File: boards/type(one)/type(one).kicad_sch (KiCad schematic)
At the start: 37 parts, among them J1 IDC-Header, J2 IDC-Header, J3 Conn_01x02, J4 Conn_01x05, J5 Conn_01x05, J6 Conn_01x03, J7 Conn_01x02, Q1 2N2907, Q2 2n2222, Q3 IRF4905, Q4 2N3904, U1 ESP32-WROOM-UE, U2 LM393, U4 LM1117T-5.0, U5 LM1117T-3.3

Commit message: creating board
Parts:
- C10: footprint (none) -> Capacitor_THT:C_Disc_D6.0mm_W2.5mm_P5.00mm
- C3: footprint Capacitor_THT:C_Rect_L16.5mm_W4.9mm_P15.00mm_MKT -> Capacitor_THT:CP_Radial_Tantal_D5.5mm_P2.50mm
- C4, C5, C6: footprint (none) -> Capacitor_THT:CP_Radial_Tantal_D5.5mm_P2.50mm
- C9: footprint (none) -> Capacitor_THT:CP_Radial_Tantal_D6.0mm_P2.50mm
- D1: footprint (none) -> Diode_THT:D_DO-35_SOD27_P7.62mm_Horizontal
- D2: value 2n5060 -> TIC106; footprint (none) -> Package_TO_SOT_THT:TO-220-3_Vertical; symbol Device:Q_SCR_AGK -> Device:Q_SCR_KAG
- F1, J3, J7: footprint (none) -> Connector_Molex:Molex_KK-254_AE-6410-02A_1x02_P2.54mm_Vertical
- J1: value IDC-Header -> IDC-Header_02x03
- J2: value IDC-Header -> IDC-Header_02x05
- J4, J5: footprint (none) -> Connector_Molex:Molex_KK-254_AE-6410-05A_1x05_P2.54mm_Vertical
- J6: footprint (none) -> Connector_Molex:Molex_KK-254_AE-6410-03A_1x03_P2.54mm_Vertical
- Q4: value 2N3904 -> 2n2222
- U4: footprint Package_SON:WSON-8-1EP_4x4mm_P0.8mm_EP1.98x3mm_ThermalVias -> Package_TO_SOT_THT:TO-220-3_Vertical
- U5: footprint Package_TO_SOT_THT:TO-220-3_Horizontal_TabDown -> Package_TO_SOT_THT:TO-220-3_Vertical
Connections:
- net +5V: no longer J2.1 (Pin_1)
- net GND: now also D2.1 (K); no longer D2.3 (K)
- net at C8.1, F1.2, Q3.1 (D): now also D2.2 (A); no longer D2.1 (A)
- net at C7.1, D1.2 (A), Q3.2 (G)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: now also D2.3 (G); no longer D2.2 (G)
- new net +3.3V: J2.1 (Pin_1)
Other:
- note added: "Input voltage VDC 9V-12V"

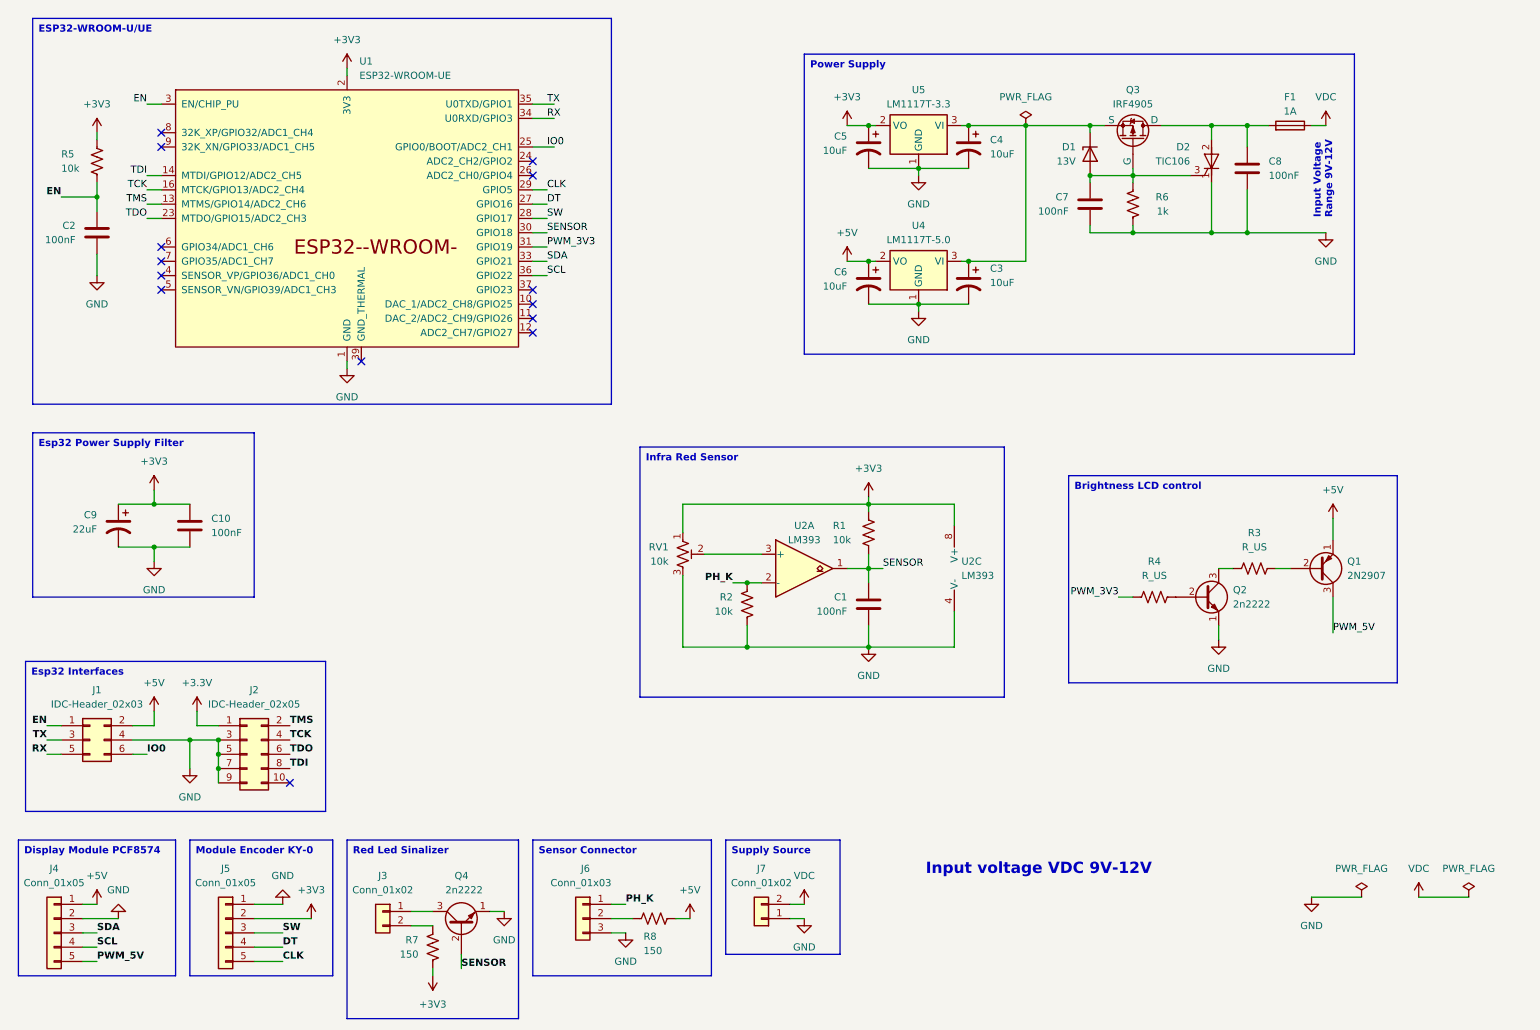
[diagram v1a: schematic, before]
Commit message: ajust sensor circuit
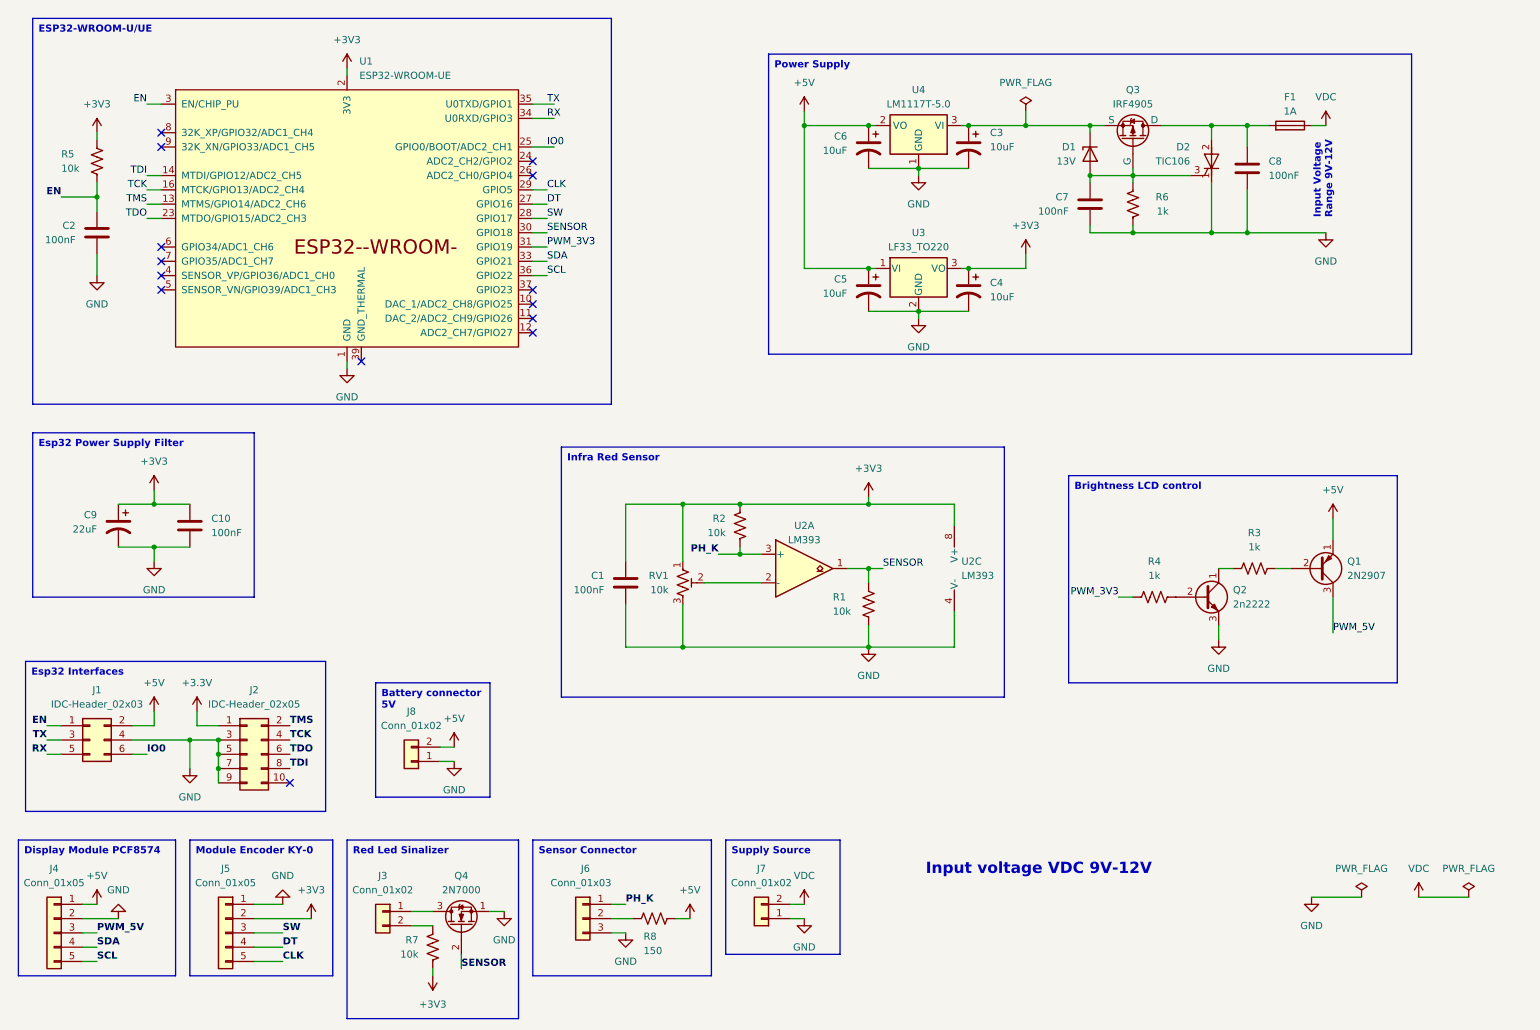
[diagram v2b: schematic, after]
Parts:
- removed Q4: 2n2222, Package_TO_SOT_THT:TO-92_Inline, symbol Transistor_BJT:2N3904
- removed U5: LM1117T-3.3, Package_TO_SOT_THT:TO-220-3_Vertical, symbol Regulator_Linear:LM1117T-3.3
- added J8: Conn_01x02, Connector_Molex:Molex_KK-254_AE-6410-02A_1x02_P2.54mm_Vertical, symbol Connector_Generic:Conn_01x02
- added Q4: 2N7000, Package_TO_SOT_THT:TO-92_Inline, symbol Transistor_FET:2N7000
- added U3: LF33_TO220, Package_TO_SOT_THT:TO-220-3_Vertical, symbol Regulator_Linear:LF33_TO220
- Q2: symbol Transistor_BJT:2N3904 -> Transistor_BJT:BC237
- R3, R4: value R_US -> 1k
- R7: value 150 -> 10k
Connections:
- net +3V3: now also C1.1, C4.1, R2.1, U3.3 (VO); no longer C5.1, R1.1
- net +5V: now also C5.1, J8.2 (Pin_2), U3.1 (VI)
- net GND: now also Q2.3 (E), R1.2, J8.1 (Pin_1), Q4.1 (S), U3.2 (GND); no longer Q2.1 (E), R2.2
- net PH_K: now also R2.2, U2.3 (+); no longer R2.1, U2.2 (-)
- net PWM_5V: now also J4.3 (Pin_3); no longer J4.5 (Pin_5)
- net SCL: now also J4.5 (Pin_5); no longer J4.4 (Pin_4)
- net SDA: now also J4.4 (Pin_4); no longer J4.3 (Pin_3)
- net SENSOR: now also R1.1, Q4.2 (G); no longer C1.1, R1.2
- net at RV1.2: now also U2.2 (-); no longer U2.3 (+)
- net at C3.1, D1.1 (K), Q3.3 (S)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: no longer C4.1
- net at R3.1: now also Q2.1 (C); no longer Q2.3 (C)
- net at J3.1 (Pin_1): now also Q4.3 (D)
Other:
- moved on the sheet: C1, C3, C4, C5, C6, R1, R2, RV1, U4

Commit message: add hysteresis on sensor
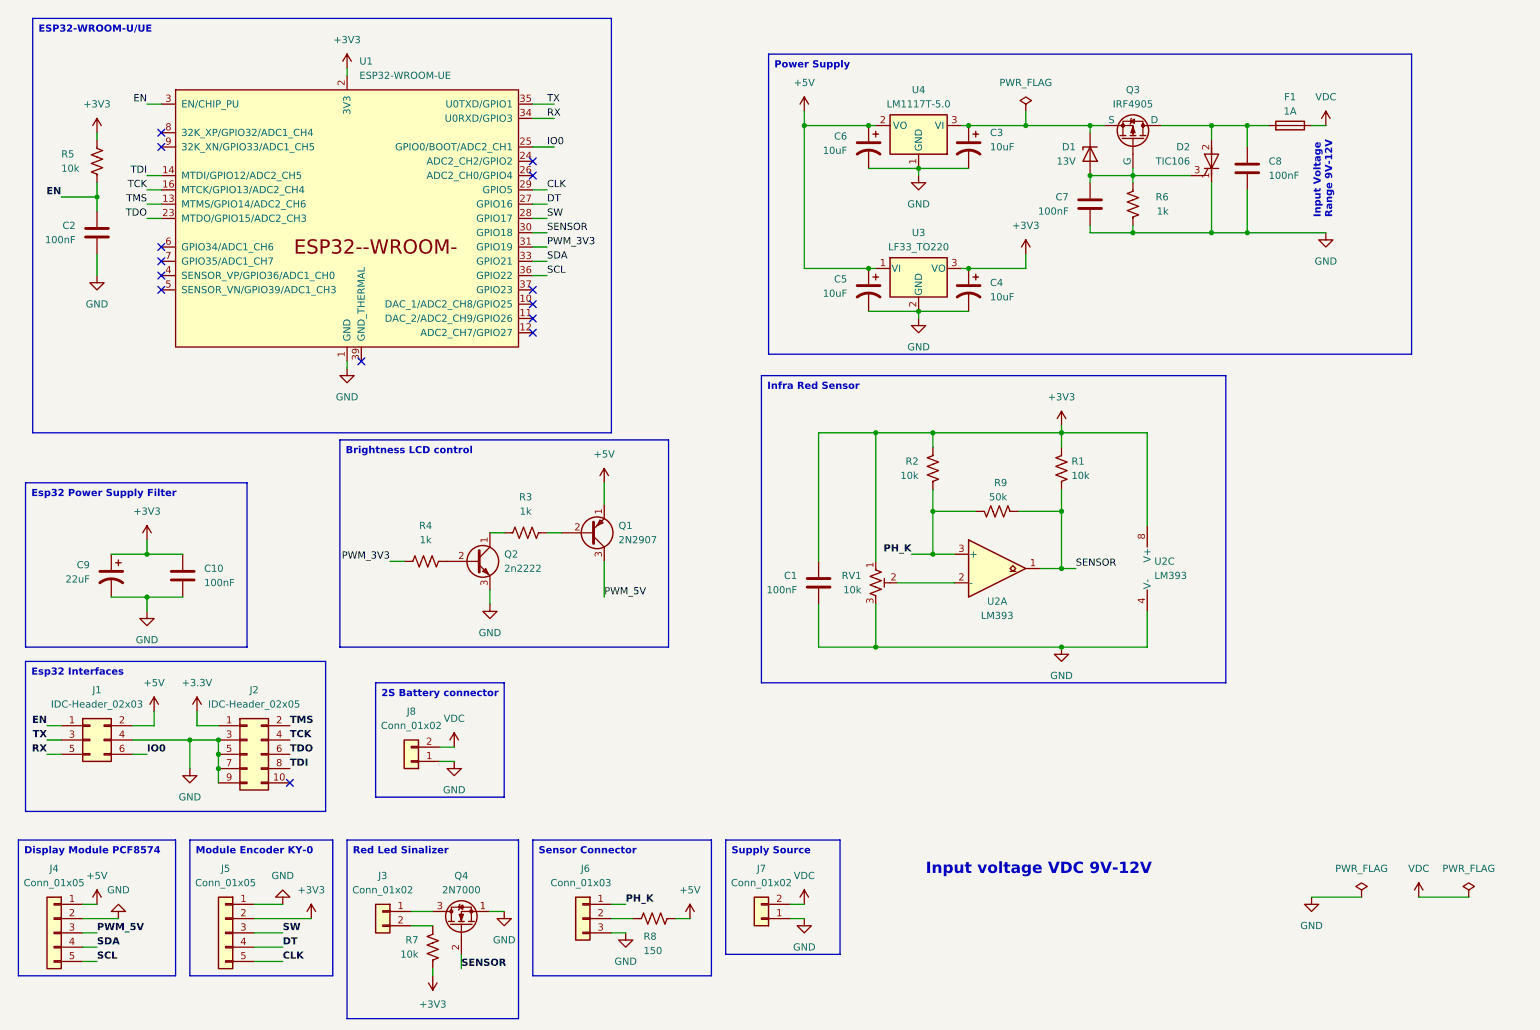
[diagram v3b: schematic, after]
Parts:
- added R9: 50k, Resistor_THT:R_Axial_DIN0207_L6.3mm_D2.5mm_P7.62mm_Horizontal, symbol Device:R_US
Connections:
- net +3V3: now also R1.1
- net +5V: no longer J8.2 (Pin_2)
- net GND: no longer R1.2
- net PH_K: now also R9.1
- net SENSOR: now also R1.2, R9.2; no longer R1.1
- net VDC: now also J8.2 (Pin_2)
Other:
- moved on the sheet: C1, C10, C9, Q1, Q2, R1, R2, R3, R4, RV1, U2A, U2C

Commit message: organize schematic
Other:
- moved on the sheet: C1, C10, C2, C3, C4, C5, C6, C7, C8, C9, D1, D2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

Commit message: Fix schematic
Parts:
- removed C4, C5, C6: 10uF, Capacitor_THT:CP_Radial_Tantal_D5.5mm_P2.50mm, symbol Device:C_Polarized_US
- removed U3: LF33_TO220, Package_TO_SOT_THT:TO-220-3_Vertical, symbol Regulator_Linear:LF33_TO220
- removed U4: LM1117T-5.0, Package_TO_SOT_THT:TO-220-3_Vertical, symbol Regulator_Linear:LM1117T-5.0
- added C6, C7: 100nF, symbol Device:C
- added C8: 220nF, Capacitor_THT:CP_Radial_Tantal_D5.5mm_P2.50mm, symbol Device:C_Polarized_US
- added RV2: 1k, Potentiometer_THT:Potentiometer_Bourns_3386X_Horizontal, symbol Device:R_Potentiometer_Trim_US
- added RV3: 10k, Potentiometer_THT:Potentiometer_Bourns_3386X_Horizontal, symbol Device:R_Potentiometer_Trim_US
- added U3: LM7805_TO220, Package_TO_SOT_THT:TO-220-3_Vertical, symbol Regulator_Linear:LM7805_TO220
- added U5: LM1117DT-ADJ, Package_TO_SOT_SMD:TO-252-3_TabPin2, symbol Regulator_Linear:LM1117DT-ADJ
- F1: value 1A -> 300mA
- renumbered C9 to C3, C10 to C4, C3 to C5, C8 to C9
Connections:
- net +3V3: now also C7.1, RV3.1, U5.2 (VO)
- net +5V: now also C6.1, C8.1, RV2.1, U3.3 (VO), U5.3 (VI); no longer R8.2
- net GND: now also C6.2, C7.2, C8.2, RV3.3, U3.2 (GND)
- net at C5.1, D1.1 (K), Q3.3 (S): now also U3.1 (VI)
- new net: RV3.2, U5.1 (ADJ)
- new net: R8.2, RV2.2
